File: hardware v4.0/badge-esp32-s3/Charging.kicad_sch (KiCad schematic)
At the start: 13 parts, among them P1 PH-2A_C2319, Q3 HL2301A, Q6 AO3424, U4 TP4056

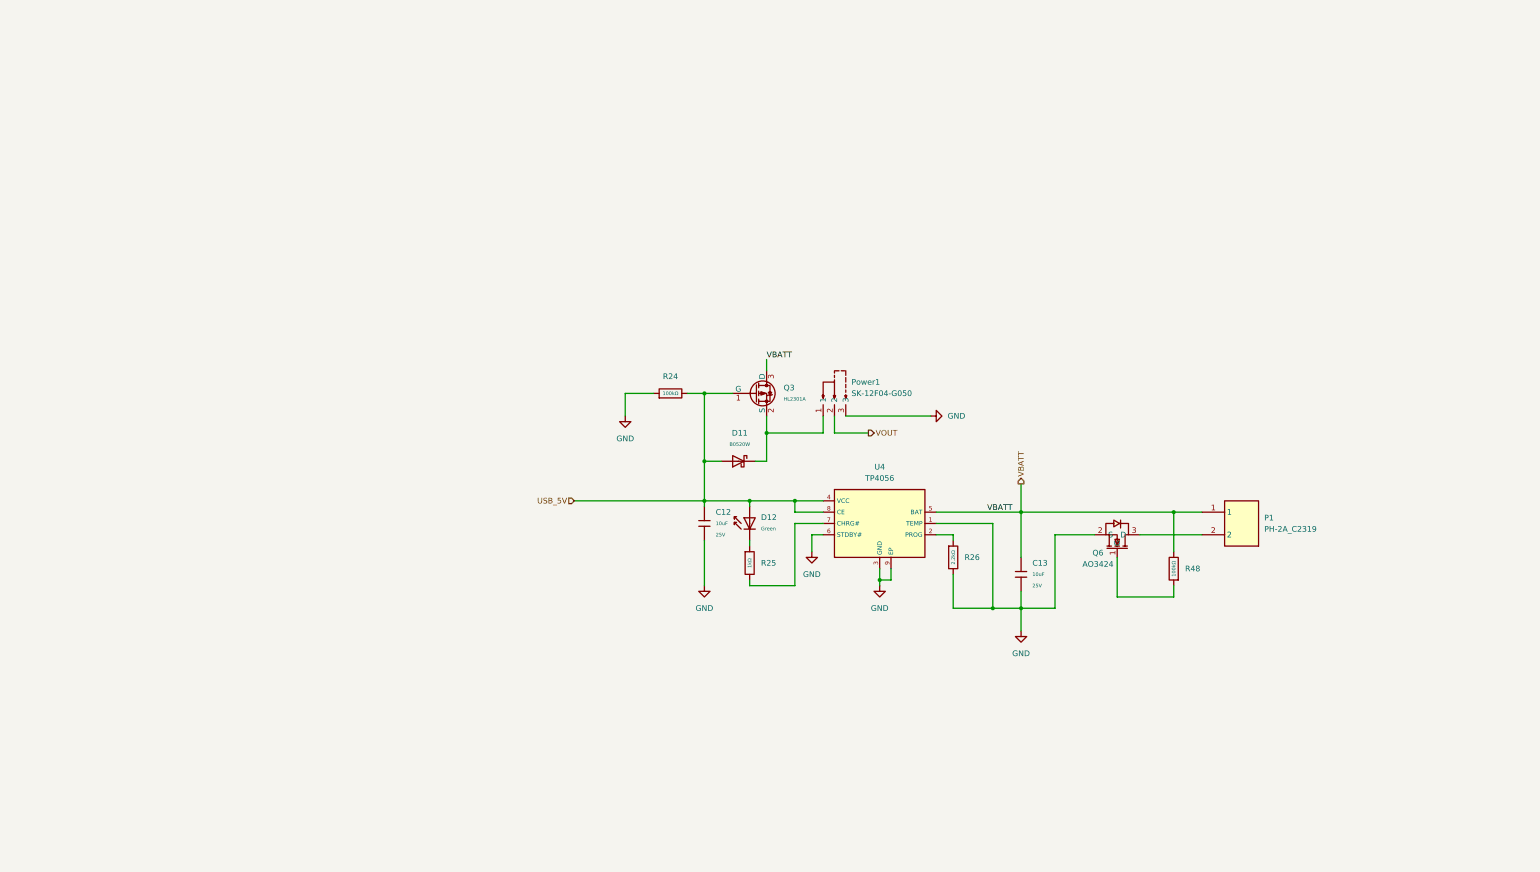
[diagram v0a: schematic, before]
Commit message: added DRD, 3.3V switching reg, and VIN
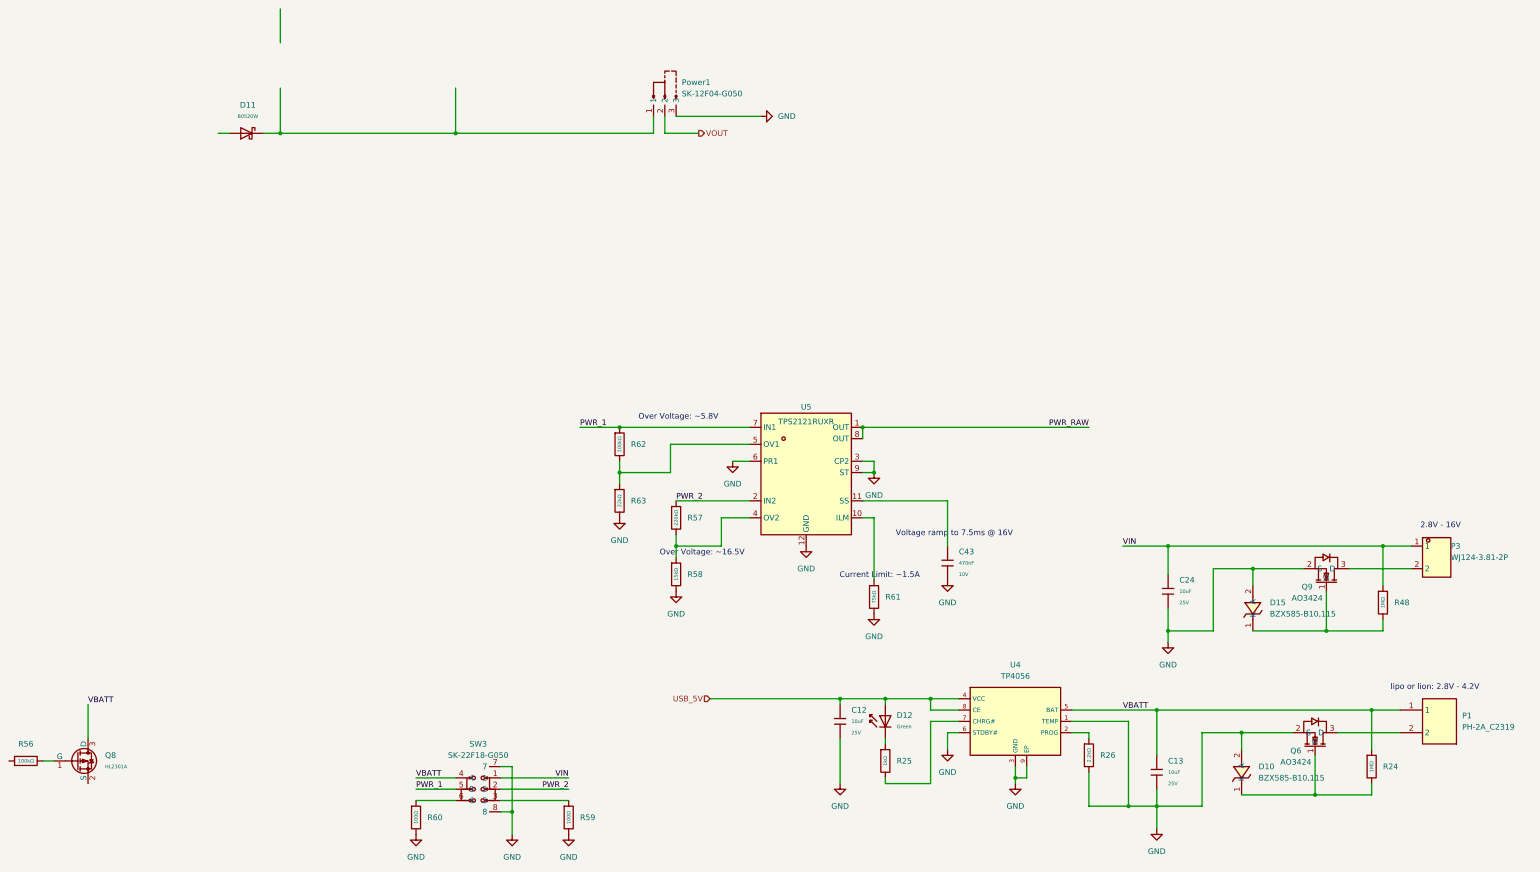
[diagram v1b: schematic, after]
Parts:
- removed Q3: HL2301A, PCM_JLCPCB:Q_SOT-23, symbol PCM_JLCPCB-Transistors:PMOS,HL2301A
- removed R24, R48: 100kΩ, PCM_JLCPCB:R_0402, symbol PCM_JLCPCB-Resistors:0402,100kΩ
- added C24: 10uF, PCM_JLCPCB:C_0603, symbol PCM_JLCPCB-Capacitors:0603,10uF,(2)
- added C43: 470nF, PCM_JLCPCB:C_0402, symbol PCM_JLCPCB-Capacitors:0402,470nF
- added D10, D15: BZX585-B10,115, lcsc-lib:SOD-523_L1.2-W0.8-LS1.6-RD, symbol lcsc-lib:BZX585-B10,115
- added P3: WJ124-3.81-2P, lcsc-lib:CONN-TH_2P-P3.81_KF124-3.81-2P, symbol lcsc-lib:WJ124-3.81-2P
- added Q8: HL2301A, PCM_JLCPCB:Q_SOT-23, symbol PCM_JLCPCB-Transistors:PMOS,HL2301A
- added Q9: AO3424, lcsc-lib:SC-59-3_L2.9-W1.6-P0.95-LS2.9-BR, symbol lcsc-lib:AO3424
- added R24, R48: 1MΩ, PCM_JLCPCB:R_0402, symbol PCM_JLCPCB-Resistors:0402,1MΩ
- added R56, R62: 100kΩ, PCM_JLCPCB:R_0402, symbol PCM_JLCPCB-Resistors:0402,100kΩ
- added R57: 220kΩ, PCM_JLCPCB:R_0402, symbol PCM_JLCPCB-Resistors:0402,220kΩ
- added R58: 15kΩ, PCM_JLCPCB:R_0402, symbol PCM_JLCPCB-Resistors:0402,15kΩ
- added R59, R60: 100Ω, PCM_JLCPCB:R_0402, symbol PCM_JLCPCB-Resistors:0402,100Ω
- added R61: 75kΩ, PCM_JLCPCB:R_0402, symbol PCM_JLCPCB-Resistors:0402,75kΩ
- added R63: 22kΩ, PCM_JLCPCB:R_0402, symbol PCM_JLCPCB-Resistors:0402,22kΩ
- added SW3: SK-22F18-G050, lcsc-lib:SW-TH_SK-22F18-G050, symbol lcsc-lib:SK-22F18-G050
- added U5: TPS2121RUXR, lcsc-lib:VQFN-HR-12_L2.5-W2.0-P0.50-BL, symbol lcsc-lib:TPS2121RUXR
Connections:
- net GND: now also C24.2, C43.2, D10.2 (A), D15.2 (A), Q9.2 (S), R58.2, R59.2, R60.2, R61.2, R63.2, SW3.7, SW3.8, U5.12 (GND), U5.3 (CP2), U5.6 (PR1), U5.9 (ST)
- net USB_5V: no longer D11.2
- net VBATT: now also Q8.3 (D), R24.1, SW3.4
- net at Q6.1 (G): now also D10.1 (K), R24.2
- new net: D15.1 (K), Q9.1 (G), R48.2
- new net: R62.2, R63.1, U5.5 (OV1)
- new net: P3.2, Q9.3 (D)
- new net: R57.2, R58.1, U5.4 (OV2)
- new net: C43.1, U5.11 (SS)
- new net: R59.1, SW3.3
- new net: R60.1, SW3.6
- new net: Q8.1 (G), R56.2
- new net: R61.1, U5.10 (ILM)
- new net PWR_1: R62.1, SW3.5, U5.7 (IN1)
- new net PWR_2: R57.1, SW3.2, U5.2 (IN2)
- new net PWR_RAW: U5.1 (OUT), U5.8 (OUT)
- new net VIN: C24.1, P3.1, R48.1, SW3.1
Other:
- note added: "2.8V - 16V"
- note added: "Current Limit: ~1.5A"
- note added: "Over Voltage: ~16.5V"
- note added: "Over Voltage: ~5.8V"
- note added: "Voltage ramp to 7.5ms @ 16V"
- note added: "lipo or lion: 2.8V - 4.2V"
- moved on the sheet: C12, C13, D11, D12, P1, Power1, Q6, R25, R26, U4
